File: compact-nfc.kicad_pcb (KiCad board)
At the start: 2 copper layers, 50 x 50 mm, 1 part

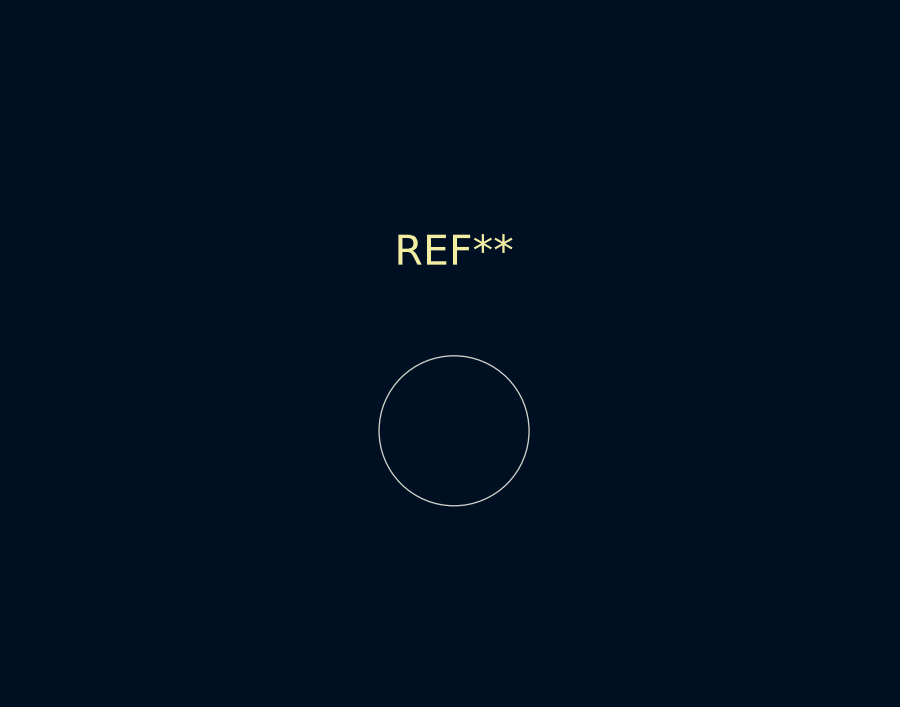
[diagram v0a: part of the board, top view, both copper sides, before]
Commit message: Add infrared barrier sensor component: footprint and schematic symbol
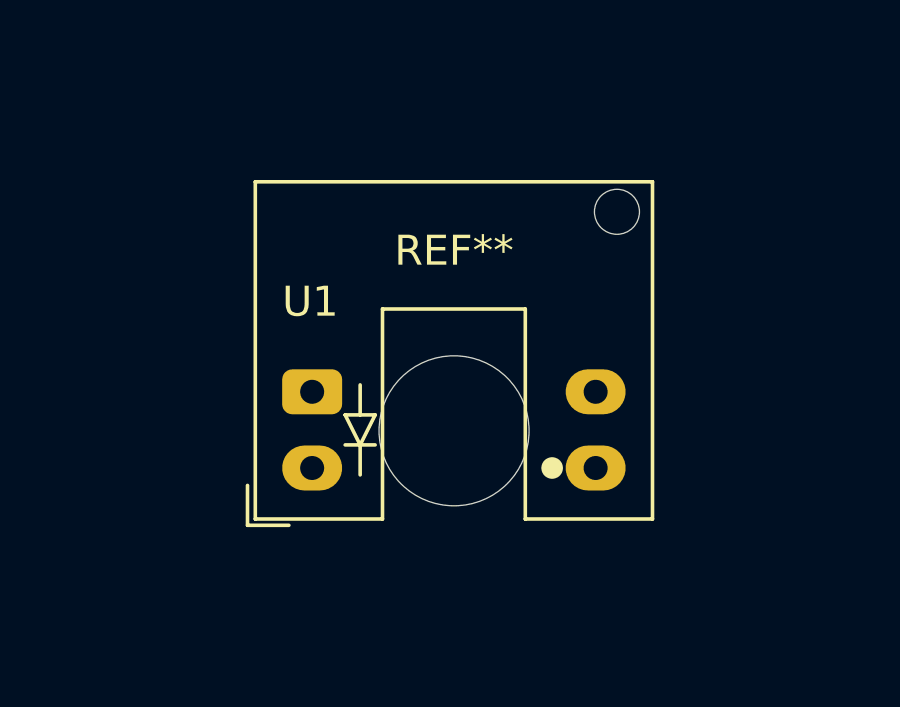
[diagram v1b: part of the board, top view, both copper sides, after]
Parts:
- added U1: ITR9702, OptoDevice_slot:Everlight_ITR9702, F.Cu at (120.3, 123.7)
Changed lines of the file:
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@@
   )
   (net 0 "")
+  (net 1 "unconnected-(U1-Pad1)")
+  (net 2 "unconnected-(U1-Pad2)")
+  (net 3 "unconnected-(U1-Pad3)")
+  (net 4 "unconnected-(U1-Pad4)")
+  (footprint "OptoDevice_slot:Everlight_ITR9702" (layer "F.Cu")
+    (at 120.27 123.7)
+    (descr "Fork-type photointerrupter (https://www.everlighteurope.com/custom/files/datasheets/DRX-0000314.pdf)")
+    (tags "Photointerrupter infrared LED")
+    (property "Sheetfile" "compact-nfc.kicad_sch")
+    (property "Sheetname" "")
+    (property "ki_description" "Photointerrupter infrared LED with photo IC, -25 to +85 degree Celsius")
+    (property "ki_keywords" "Photointerrupter opto interrupter infrared LED fast response time infrared 940nm 5mm gap")
+    (attr through_hole)
+    (fp_text reference "U1" (at -1 -3 180) (layer "F.SilkS")
+        (effects (font (size 1 1) (thickness 0.15)) (justify left))
+    )
+    (fp_text value "ITR9702" (at 5 5.77) (layer "F.Fab")
+        (effects (font (size 1 1) (thickness 0.15)))
+    )
+    (fp_text user "${REFERENCE}" (at 5 1.27 180) (layer "F.Fab")
+        (effects (font (size 1 1) (thickness 0.15)))
+    )
+    (fp_line (start -2.155 4.45) (end -2.155 3.12)
+      (stroke (width 0.12) (type solid)) (layer "F.SilkS"))
+    (fp_line (start -2.155 4.45) (end -0.775 4.45)
+      (stroke (width 0.12) (type solid)) (layer "F.SilkS"))
+    (fp_line (start -1.895 -7) (end 11.345 -7)
+      (stroke (width 0.12) (type solid)) (layer "F.SilkS"))
+    (fp_line (start -1.895 4.24) (end -1.895 -7)
+      (stroke (width 0.12) (type solid)) (layer "F.SilkS"))
+    (fp_line (start 1.1 0.77) (end 1.6 1.77)
+      (stroke (width 0.12) (type solid)) (layer "F.SilkS"))
+    (fp_line (start 1.6 0.77) (end 1.6 -0.23)
+      (stroke (width 0.12) (type solid)) (layer "F.SilkS"))
+    (fp_line (start 1.6 1.77) (end 1.6 2.77)
+      (stroke (width 0.12) (type solid)) (layer "F.SilkS"))
+    (fp_line (start 1.6 1.77) (end 2.1 0.77)
+      (stroke (width 0.12) (type solid)) (layer "F.SilkS"))
+    (fp_line (start 2.1 0.77) (end 1.1 0.77)
+      (stroke (width 0.12) (type solid)) (layer "F.SilkS"))
+    (fp_line (start 2.1 1.77) (end 1.1 1.77)
+      (stroke (width 0.12) (type solid)) (layer "F.SilkS"))
+    (fp_line (start 2.345 4.24) (end -1.895 4.24)
+      (stroke (width 0.12) (type solid)) (layer "F.SilkS"))
+    (fp_line (start 2.345 4.24) (end 2.345 -2.76)
+      (stroke (width 0.12) (type solid)) (layer "F.SilkS"))
+    (fp_line (start 7.105 -2.76) (end 2.345 -2.76)
+      (stroke (width 0.12) (type solid)) (layer "F.SilkS"))
+    (fp_line (start 7.105 4.24) (end 7.105 -2.76)
+      (stroke (width 0.12) (type solid)) (layer "F.SilkS"))
+    (fp_line (start 11.345 -7) (end 11.345 4.24)
+      (stroke (width 0.12) (type solid)) (layer "F.SilkS"))
+    (fp_line (start 11.345 4.24) (end 7.105 4.24)
+      (stroke (width 0.12) (type solid)) (layer "F.SilkS"))
+    (fp_circle (center 8 2.54) (end 8.3 2.54)
+      (stroke (width 0.12) (type solid)) (fill solid) (layer "F.SilkS"))
+    (fp_line (start -5 1.27) (end 13 1.27)
+      (stroke (width 0.1) (type default)) (layer "Cmts.User"))
+    (fp_line (start 0 -12) (end 0 12)
+      (stroke (width 0.1) (type default)) (layer "Cmts.User"))
+    (fp_line (start 9.45 -12) (end 9.45 12)
+      (stroke (width 0.1) (type default)) (layer "Cmts.User"))
+    (fp_line (start -2.025 -7.13) (end 11.475 -7.13)
+      (stroke (width 0.05) (type solid)) (layer "F.CrtYd"))
+    (fp_line (start -2.025 4.37) (end -2.025 -7.13)
+      (stroke (width 0.05) (type solid)) (layer "F.CrtYd"))
+    (fp_line (start 11.475 -7.13) (end 11.475 4.37)
+      (stroke (width 0.05) (type solid)) (layer "F.CrtYd"))
+    (fp_line (start 11.475 4.37) (end -2.025 4.37)
+      (stroke (width 0.05) (type solid)) (layer "F.CrtYd"))
+    (fp_line (start -1.775 -6.88) (end 11.225 -6.88)
+      (stroke (width 0.1) (type solid)) (layer "F.Fab"))
+    (fp_line (start -1.775 3.12) (end -1.775 -6.88)
+      (stroke (width 0.1) (type solid)) (layer "F.Fab"))
+    (fp_line (start -1.775 3.12) (end -0.775 4.12)
+      (stroke (width 0.1) (type solid)) (layer "F.Fab"))
+    (fp_line (start 1.1 0.77) (end 1.6 1.77)
+      (stroke (width 0.1) (type solid)) (layer "F.Fab"))
+    (fp_line (start 1.6 0.77) (end 1.6 -0.23)
+      (stroke (width 0.1) (type solid)) (layer "F.Fab"))
+    (fp_line (start 1.6 1.77) (end 1.6 2.77)
+      (stroke (width 0.1) (type solid)) (layer "F.Fab"))
+    (fp_line (start 1.6 1.77) (end 2.1 0.77)
+      (stroke (width 0.1) (type solid)) (layer "F.Fab"))
+    (fp_line (start 2.1 1.77) (end 1.1 1.77)
+      (stroke (width 0.1) (type solid)) (layer "F.Fab"))
+    (fp_line (start 2.225 -2.88) (end 2.225 4.12)
+      (stroke (width 0.1) (type solid)) (layer "F.Fab"))
+    (fp_line (start 2.225 -2.88) (end 7.225 -2.88)
+      (stroke (width 0.1) (type solid)) (layer "F.Fab"))
+    (fp_line (start 2.225 4.12) (end -0.775 4.12)
+      (stroke (width 0.1) (type solid)) (layer "F.Fab"))
+    (fp_line (start 2.3 0.77) (end 1.3 0.77)
+      (stroke (width 0.1) (type solid)) (layer "F.Fab"))
+    (fp_line (start 7.225 -2.88) (end 7.225 4.12)
+      (stroke (width 0.1) (type solid)) (layer "F.Fab"))
+    (fp_line (start 7.225 4.12) (end 11.225 4.12)
+      (stroke (width 0.1) (type solid)) (layer "F.Fab"))
+    (fp_line (start 11.225 -6.88) (end 11.225 4.12)
+      (stroke (width 0.1) (type solid)) (layer "F.Fab"))
+    (pad "" np_thru_hole circle (at 10.16 -6 90) (size 1.5 1.5) (drill 1.5) (layers "F&B.Cu" "*.Mask"))
+    (pad "1" thru_hole roundrect (at 0 0 90) (size 1.5 2) (drill 0.8) (layers "*.Cu" "*.Mask") (roundrect_rratio 0.227)
+      (net 1 "unconnected-(U1-Pad1)") (pintype "passive"))
+    (pad "2" thru_hole oval (at 0 2.54 90) (size 1.5 2) (drill 0.8) (layers "*.Cu" "*.Mask")
+      (net 2 "unconnected-(U1-Pad2)") (pintype "passive"))
+    (pad "3" thru_hole oval (at 9.45 2.54 90) (size 1.5 2) (drill 0.8) (layers "*.Cu" "*.Mask")
+      (net 3 "unconnected-(U1-Pad3)") (pintype "open_collector"))
+    (pad "4" thru_hole oval (at 9.45 0 90) (size 1.5 2) (drill 0.8) (layers "*.Cu" "*.Mask")
+      (net 4 "unconnected-(U1-Pad4)") (pintype "open_emitter"))
+    (model "${KICAD6_3DMODEL_DIR}/OptoDevice.3dshapes/Everlight_ITR9608-F.wrl"
+      (offset (xyz 0 0 0))
+      (scale (xyz 1 1 1))
+      (rotate (xyz 0 0 0))
+    )
+  )
   (footprint "MountingHole:MountingHole_5mm" (layer "F.Cu")
     (at 125 125)

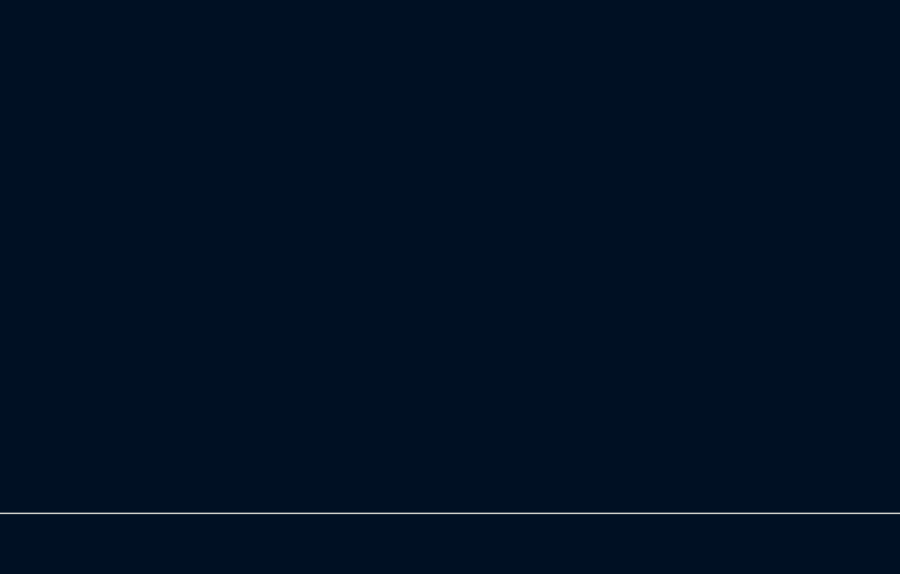
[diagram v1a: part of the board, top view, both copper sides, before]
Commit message: Add NFC chip and coil patterns for PCB
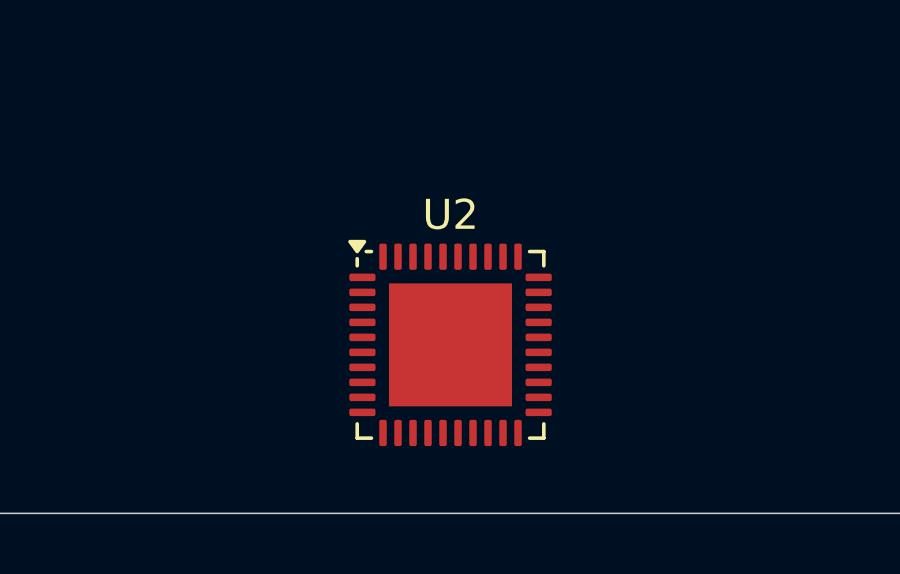
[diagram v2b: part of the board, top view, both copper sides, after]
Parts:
- added U2: PN5321A3HN_C1xx, Package_DFN_QFN:HVQFN-40-1EP_6x6mm_P0.5mm_EP4.1x4.1mm, F.Cu at (124.1, 144.4)

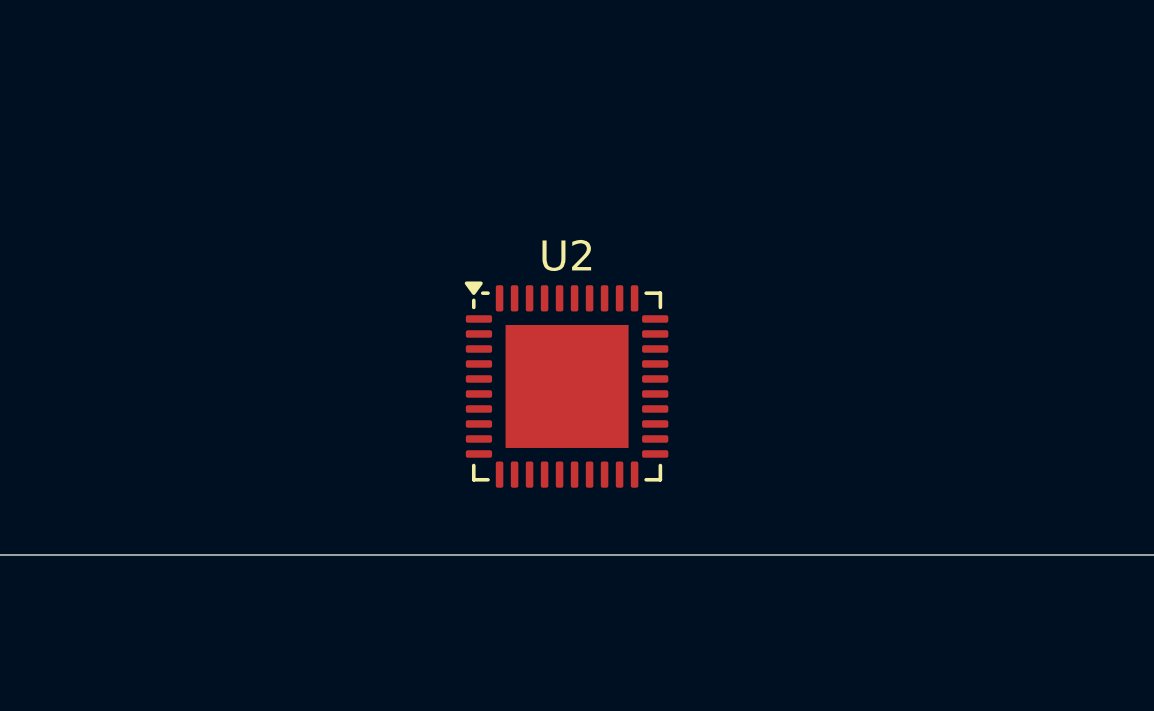
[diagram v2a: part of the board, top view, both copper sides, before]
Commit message: Add coupling components to NFC antenna
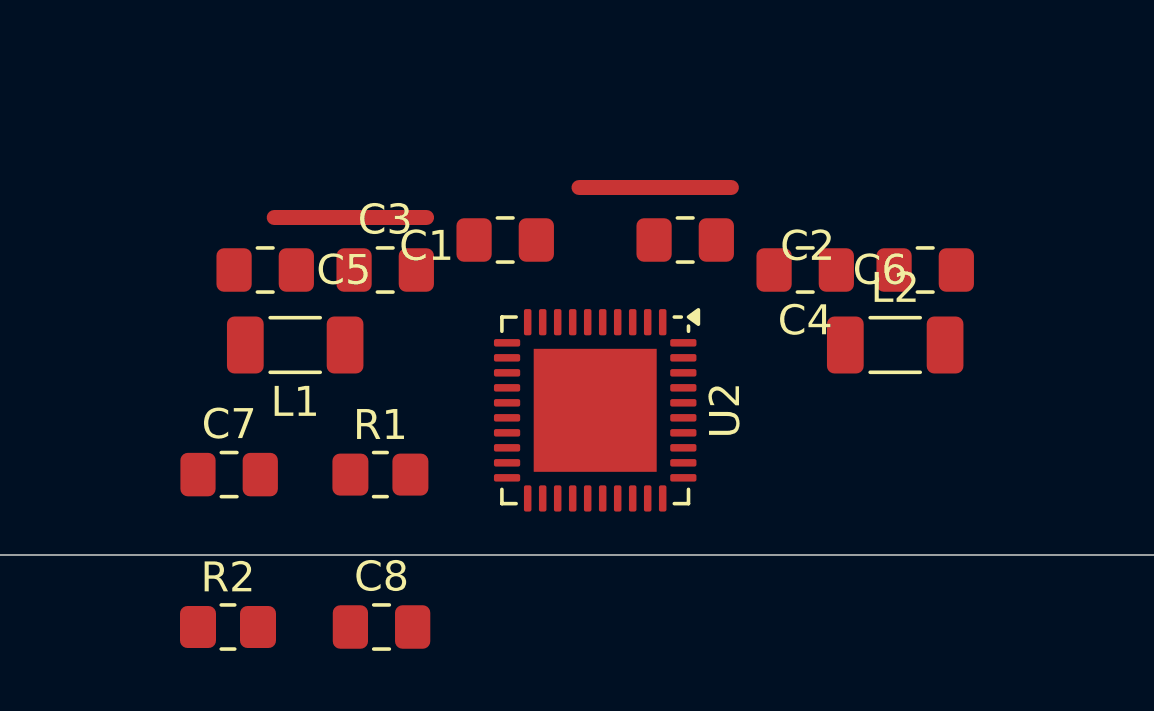
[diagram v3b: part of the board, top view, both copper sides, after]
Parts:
- added C1: C, Capacitor_SMD:C_0805_2012Metric_Pad1.18x1.45mm_HandSolder, F.Cu at (122.0, 139.5)
- added C2: C, Capacitor_SMD:C_0805_2012Metric_Pad1.18x1.45mm_HandSolder, F.Cu at (128.0, 139.5)
- added C3: C, Capacitor_SMD:C_0805_2012Metric_Pad1.18x1.45mm_HandSolder, F.Cu at (118.0, 140.5)
- added C4: C, Capacitor_SMD:C_0805_2012Metric_Pad1.18x1.45mm_HandSolder, F.Cu at (132.0, 140.5)
- added C5: C, Capacitor_SMD:C_0805_2012Metric_Pad1.18x1.45mm_HandSolder, F.Cu at (114.0, 140.5)
- added C6: C, Capacitor_SMD:C_0805_2012Metric_Pad1.18x1.45mm_HandSolder, F.Cu at (136.0, 140.5)
- added C7: C, Capacitor_SMD:C_0805_2012Metric_Pad1.18x1.45mm_HandSolder, F.Cu at (112.8, 147.3)
- added C8: C, Capacitor_SMD:C_0805_2012Metric_Pad1.18x1.45mm_HandSolder, F.Cu at (117.9, 152.4)
- added L1: L, Inductor_SMD:L_1206_3216Metric_Pad1.22x1.90mm_HandSolder, F.Cu at (115.0, 143.0)
- added L2: L, Inductor_SMD:L_1206_3216Metric_Pad1.22x1.90mm_HandSolder, F.Cu at (135.0, 143.0)
- added R1: R, Resistor_SMD:R_0805_2012Metric_Pad1.20x1.40mm_HandSolder, F.Cu at (117.8, 147.3)
- added R2: R, Resistor_SMD:R_0805_2012Metric_Pad1.20x1.40mm_HandSolder, F.Cu at (112.8, 152.4)
- moved U2 1.23 mm to (125.0, 145.2), turned to -90 degrees
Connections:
- U2 pad 10: unconnected-(U2-RX-Pad10) -> Net-(U2-RX)
- U2 pad 4: unconnected-(U2-TX1-Pad4) -> Net-(U2-TX1)
- U2 pad 6: unconnected-(U2-TX2-Pad6) -> Net-(U2-TX2)
- U2 pad 9: unconnected-(U2-VMID-Pad9) -> Net-(U2-VMID)
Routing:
- net (no net): track 0.00 -> 10.2 mm

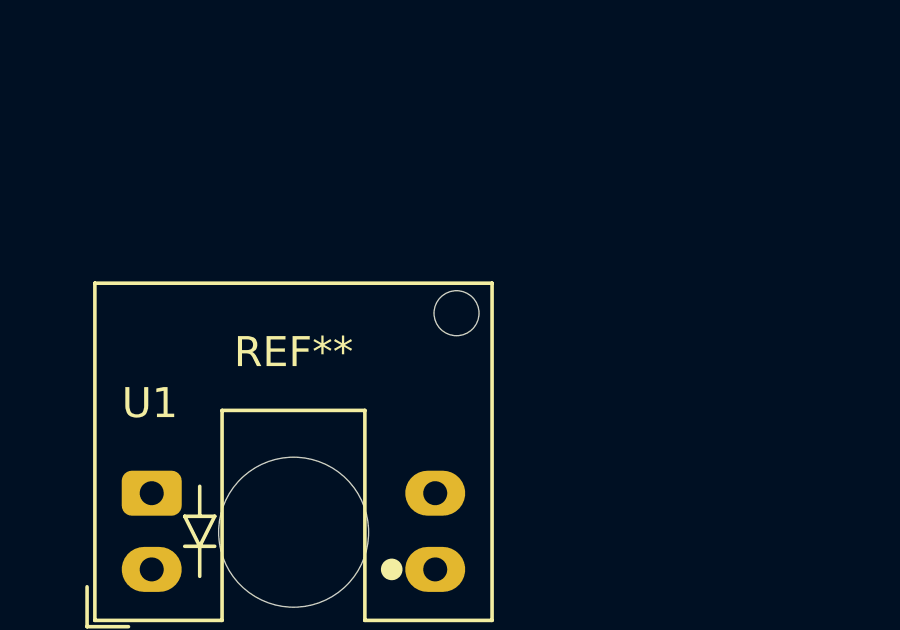
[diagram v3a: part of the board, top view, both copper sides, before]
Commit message: Update optical sensor fixation pin
- Modify Everlight ITR9702 footprint (Everlight_ITR9702.kicad_mod)
- Update PCB layout and schematic accordingly
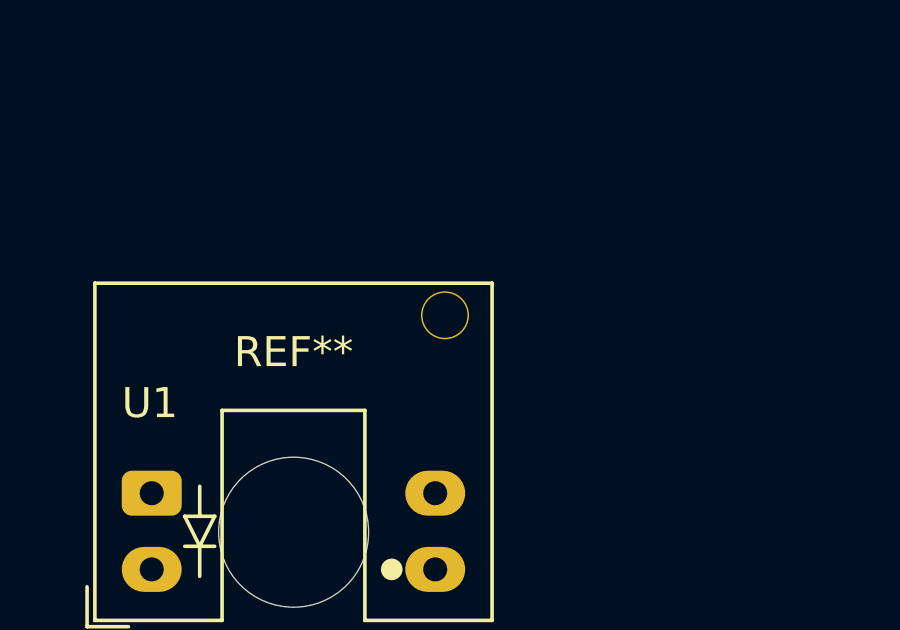
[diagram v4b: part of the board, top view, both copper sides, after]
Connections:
- U2 pad 1: unconnected-(U2-DVSS-Pad1) -> GND
- U2 pad 11: Net-(U2-AVSS-Pad11) -> GND
- U2 pad 18: unconnected-(U2-TESTEN-Pad18) -> GND
- U2 pad 3: unconnected-(U2-TVSS1-Pad3) -> GND
- U2 pad 41: Net-(U2-AVSS-Pad11) -> GND
- U2 pad 7: unconnected-(U2-TVSS2-Pad7) -> GND
